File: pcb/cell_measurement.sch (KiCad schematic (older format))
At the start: 26 parts

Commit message: finished cell tab board
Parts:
- removed TP? (x9): Sense Pad, symbol Connector:TestPoint_Alt
- added C1: 100p, symbol Device:C_Small
- added C2: 0.1u, symbol Device:C_Small
- added J12: Taps 6-8, Connector_PinHeader_2.54mm:PinHeader_1x04_P2.54mm_Vertical, symbol Connector:Conn_01x04_Male
- added J13: Taps 0-5, Connector_PinHeader_2.54mm:PinHeader_1x05_P2.54mm_Vertical, symbol Connector:Conn_01x05_Male
- added R1, R3: 100, symbol Device:R_US
- added R2: R_US, symbol Device:R_US
- C10, C4, C5, C6, C7, C8, C9: renamed from C?; footprint (none) -> Capacitor_SMD:C_0805_2012Metric
- C3: renamed from C?; value 200n -> 220n; footprint (none) -> Capacitor_SMD:C_0805_2012Metric
- R10, R11, R4, R5, R6, R7, R8, R9: renamed from R?; footprint (none) -> Resistor_SMD:R_0805_2012Metric
- gave numbers to parts that had none: 1
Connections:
- wire segments 76 -> 111

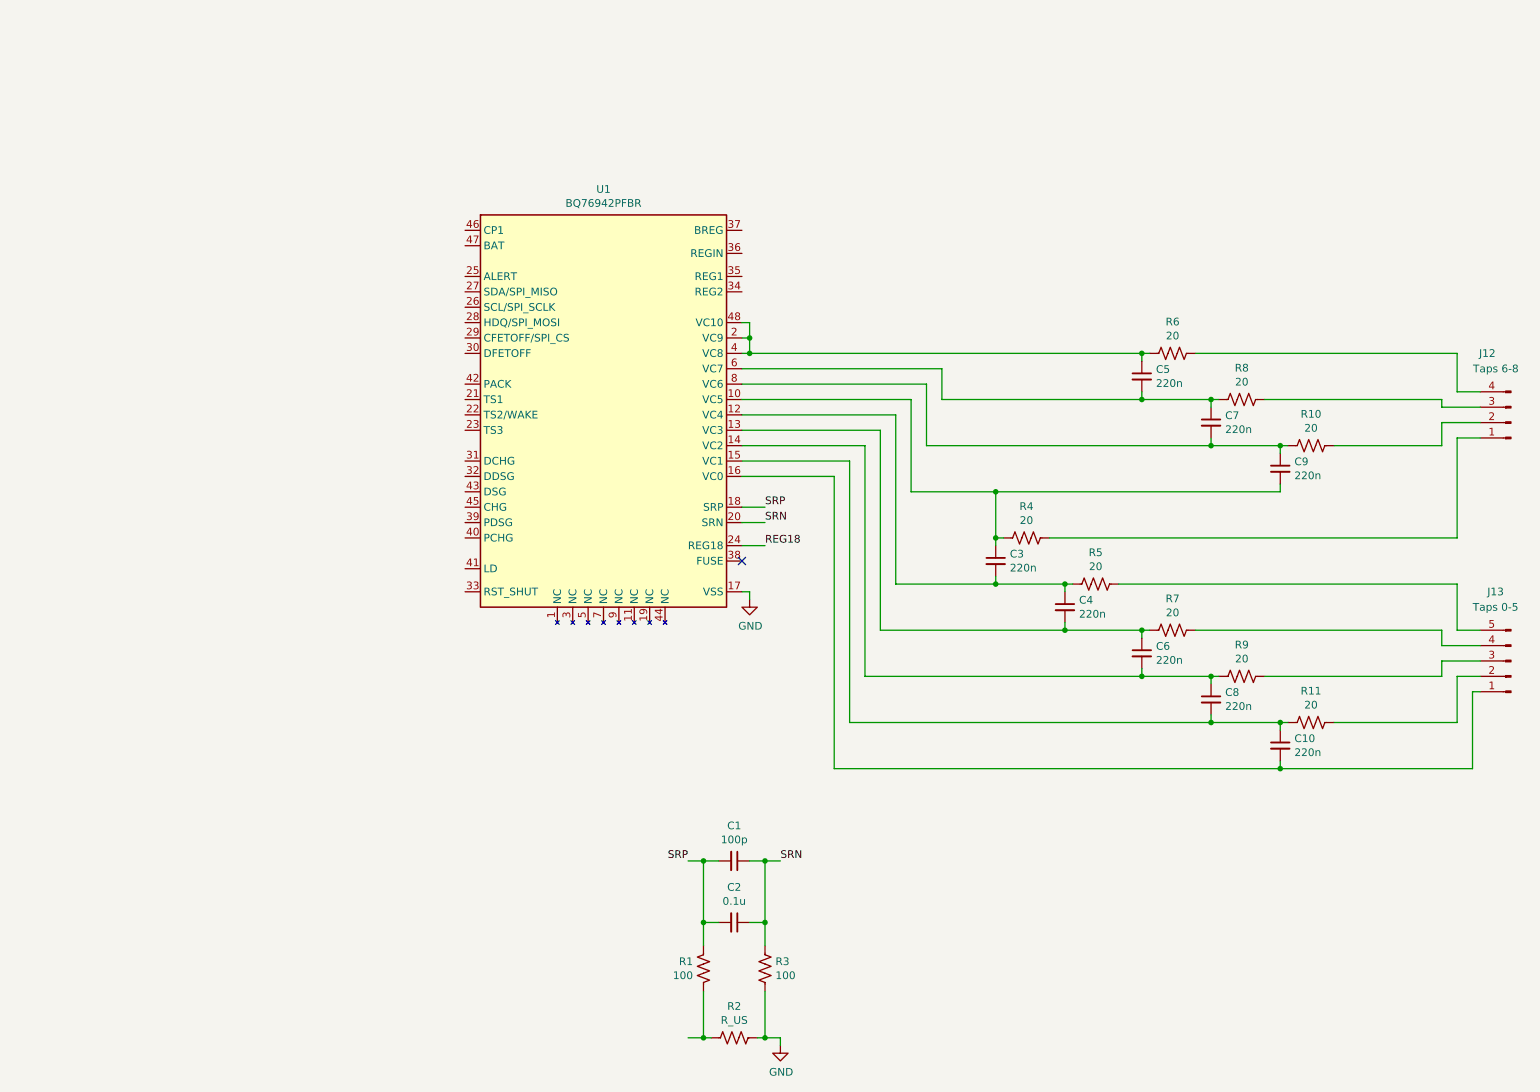
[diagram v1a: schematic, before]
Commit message: AFE mostly complete
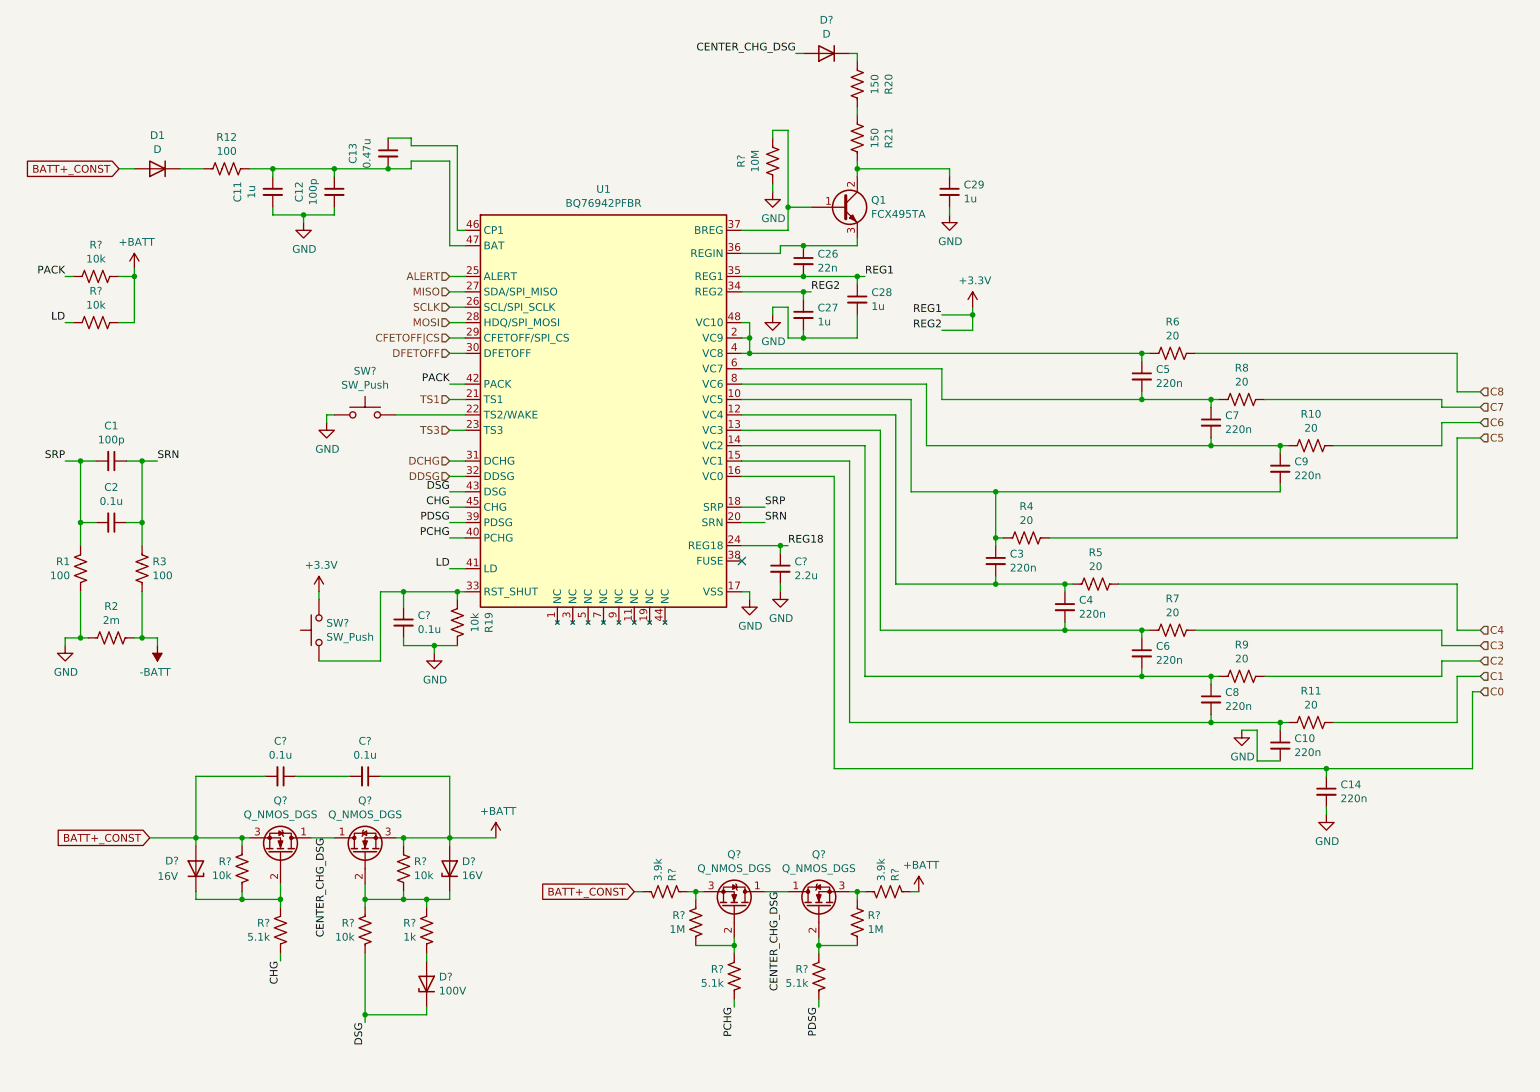
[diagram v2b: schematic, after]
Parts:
- removed J12: Taps 6-8, Connector_PinHeader_2.54mm:PinHeader_1x04_P2.54mm_Vertical, symbol Connector:Conn_01x04_Male
- removed J13: Taps 0-5, Connector_PinHeader_2.54mm:PinHeader_1x05_P2.54mm_Vertical, symbol Connector:Conn_01x05_Male
- added C11: 1u, symbol Device:C_Small
- added C12: 100p, symbol Device:C_Small
- added C13: 0.47u, symbol Device:C_Small
- added C14: 220n, Capacitor_SMD:C_0805_2012Metric, symbol Device:C_Small
- added C26: 22n, Capacitor_SMD:C_0805_2012Metric, symbol Device:C_Small
- added C27, C28, C29: 1u, Capacitor_SMD:C_0805_2012Metric, symbol Device:C_Small
- added C?: 0.1u, Capacitor_SMD:C_0805_2012Metric, symbol Device:C_Small
- added C?: 2.2u, Capacitor_SMD:C_0805_2012Metric, symbol Device:C_Small
- added C? (x2): 0.1u, symbol Device:C_Small
- added D1, D?: D, symbol Device:D
- added D? (x2): 16V, symbol Device:D_Zener
- added D?: 100V, symbol Device:D_Zener
- added Q1: FCX495TA, symbol Device:Q_NPN_BCE
- added Q? (x4): Q_NMOS_DGS, symbol Device:Q_NMOS_DGS
- added R12: 100, Resistor_SMD:R_0805_2012Metric, symbol Device:R_US
- added R19, R? (x2): 10k, Resistor_SMD:R_0805_2012Metric, symbol Device:R_US
- added R20, R21: 150, Resistor_SMD:R_0805_2012Metric, symbol Device:R_US
- added R? (x3): 10k, symbol Device:R_US
- added R? (x3): 5.1k, symbol Device:R_US
- added R?: 10M, Resistor_SMD:R_0805_2012Metric, symbol Device:R_US
- added R?: 1k, symbol Device:R_US
- added R? (x2): 1M, symbol Device:R_US
- added R? (x2): 3.9k, symbol Device:R_US
- added SW? (x2): SW_Push, symbol Switch:SW_Push
- R2: value R_US -> 2m
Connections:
- net GND: now also C10.2, R1.1, R2.2, C11.2, C12.2, C14.2, C27.2, C28.2, C29.2, C?.2, C?.2, R19.2, R?.2, SW?.1; no longer R2.1, R3.2
- net REG18: now also C?.1
- net C0: now reaches U1.16 (VC0)
- net C0: now also C14.1; no longer C10.2
- net TS1: now reaches U1.21 (TS1)
- net at U1.22 (TS2/WAKE): now also SW?.2
- net TS3: now reaches U1.23 (TS3)
- net ALERT: now reaches U1.25 (ALERT)
- net SCLK: now reaches U1.26 (SCL/SPI_SCLK)
- net MISO: now reaches U1.27 (SDA/SPI_MISO)
- net MOSI: now reaches U1.28 (HDQ/SPI_MOSI)
- net CFETOFF|CS: now reaches U1.29 (CFETOFF/SPI_CS)
- net DFETOFF: now reaches U1.30 (DFETOFF)
- net DCHG: now reaches U1.31 (DCHG)
- net DDSG: now reaches U1.32 (DDSG)
- net at U1.33 (RST_SHUT): now also C?.1, R19.1, SW?.2
- net +3V3: now reaches U1.34 (REG2)
- net +3V3: now also U1.35 (REG1), C26.2, C27.1, C28.1, SW?.1
- net at U1.36 (REGIN): now also C26.1, Q1.3 (E)
- net at U1.37 (BREG): now also Q1.1 (B), R?.1
- net PDSG: now reaches U1.39 (PDSG)
- net PDSG: now also R?.1
- net PCHG: now reaches U1.40 (PCHG)
- net PCHG: now also R?.1
- net LD: now reaches U1.41 (LD)
- net LD: now also R?.2
- net PACK: now reaches U1.42 (PACK)
- net PACK: now also R?.2
- net DSG: now reaches U1.43 (DSG)
- net DSG: now also D?.1 (K), R?.1
- net CHG: now reaches U1.45 (CHG)
- net CHG: now also R?.1
- net at U1.46 (CP1): now also C13.1
- net at U1.47 (BAT): now also C11.1, C12.1, C13.2, R12.1
- net C8: now reaches R6.1
- net C7: now reaches R8.1
- net C5: now reaches R4.1
- net C4: now reaches R5.1
- net C3: now reaches R7.1
- net C2: now reaches R9.1
- net C6: now reaches R10.1
- net C1: now reaches R11.1
- new net: D1.1 (K), R12.2
- new net: D?.1 (K), R20.2
- new net: D?.1 (K), Q?.2 (G), R?.1, R?.2, R?.2
- new net: D?.1 (K), Q?.2 (G), R?.1, R?.2
- new net: C29.1, Q1.2 (C), R21.1
- new net: R20.1, R21.2
- new net: C?.1, C?.2
- new net: D?.2 (A), R?.1
- new net: Q?.2 (G), R?.1, R?.2 (x2)
- new net: Q?.3 (S), R?.2, R?.2
- new net: Q?.3 (S), R?.1, R?.2
- new net +BATT: C?.1, D?.2 (A), Q?.3 (S), R?.1, R?.1, R?.2, R?.2
- new net -BATT: R2.1, R3.2
- new net BATT+_CONST: C?.2, D1.2 (A), D?.2 (A), Q?.3 (S), R?.1, R?.2
- new net CENTER_CHG_DSG: D?.2 (A), Q?.1 (D), Q?.1 (D), Q?.1 (D), Q?.1 (D)
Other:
- moved on the sheet: C1, C2, R1, R2, R3

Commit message: microcontroller added
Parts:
- removed C27: 1u, Capacitor_SMD:C_0805_2012Metric, symbol Device:C_Small
- removed C?: 0.1u, Capacitor_SMD:C_0805_2012Metric, symbol Device:C_Small
- removed Q? (x2): Q_NMOS_DGS, symbol Device:Q_NMOS_DGS
- removed SW?: SW_Push, symbol Switch:SW_Push
- added C?: 0.1u, Capacitor_SMD:C_0805_2012Metric, symbol Device:C_Small
- added Q4, Q5: ZXMP10A13FTA, Package_TO_SOT_SMD:SOT-23, symbol Device:Q_PMOS_DGS
- C1, C11, C12, C13, C2: footprint (none) -> Capacitor_SMD:C_0805_2012Metric
- C32, C33: renamed from C?; footprint (none) -> Capacitor_SMD:C_0805_2012Metric
- Q2, Q3: renamed from Q?; value Q_NMOS_DGS -> CSD19506KTT; footprint (none) -> Package_TO_SOT_SMD:TO-263-2; symbol Device:Q_NMOS_DGS -> Device:Q_NMOS_GDS
- R1, R3: footprint (none) -> Resistor_SMD:R_0805_2012Metric
- R2: footprint (none) -> Resistor_SMD:R_1210_3225Metric
- R24, R25, R26, R27, R28, R29, R30, R31, R33, R34, R35: renamed from R?; footprint (none) -> Resistor_SMD:R_0805_2012Metric
- gave numbers to parts that had none: 9
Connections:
- net +3V3: no longer U1.34 (REG2)
- net CENTER_CHG_DSG: now also Q2.2 (D), Q3.2 (D), Q4.3 (S), Q5.3 (S); no longer Q2.1 (D), Q3.1 (D)
- net GND: now also C?.2
- net at C5.1, R6.2, U1.48 (VC10): no longer U1.2 (VC9), U1.4 (VC8)
- net at SW2.2, U1.22 (TS2/WAKE): now also C?.1
- net RST_SHUT: now reaches R19.1, U1.33 (RST_SHUT)
- net at C5.2, C7.1, R8.2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: now also U1.2 (VC9), U1.4 (VC8)
- net at D4.1 (K), R26.2, R27.1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: now also Q3.1 (G); no longer Q3.2 (G)
- net at D2.1 (K), R24.1, R25.2: now also Q2.1 (G); no longer Q2.2 (G)
- net at R30.1, R31.2: now also Q4.2 (G)
- net at R29.2, R30.2: now also Q4.1 (D)
- net at R33.2, R34.1: now also Q5.2 (G)
- net at R34.2, R35.1: now also Q5.1 (D)
- no-connect marks 1 -> 2
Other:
- moved on the sheet: C28
